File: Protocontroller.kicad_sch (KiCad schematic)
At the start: 37 parts, among them U1 AP2112K-3.3TRG1, U2 PM254-1-14-Z-8.5, U3 PM254-1-14-Z-8.5, U4 74245PW, U5 74245PW, U6 74374PW, U8 HC-JN254-2-08-W

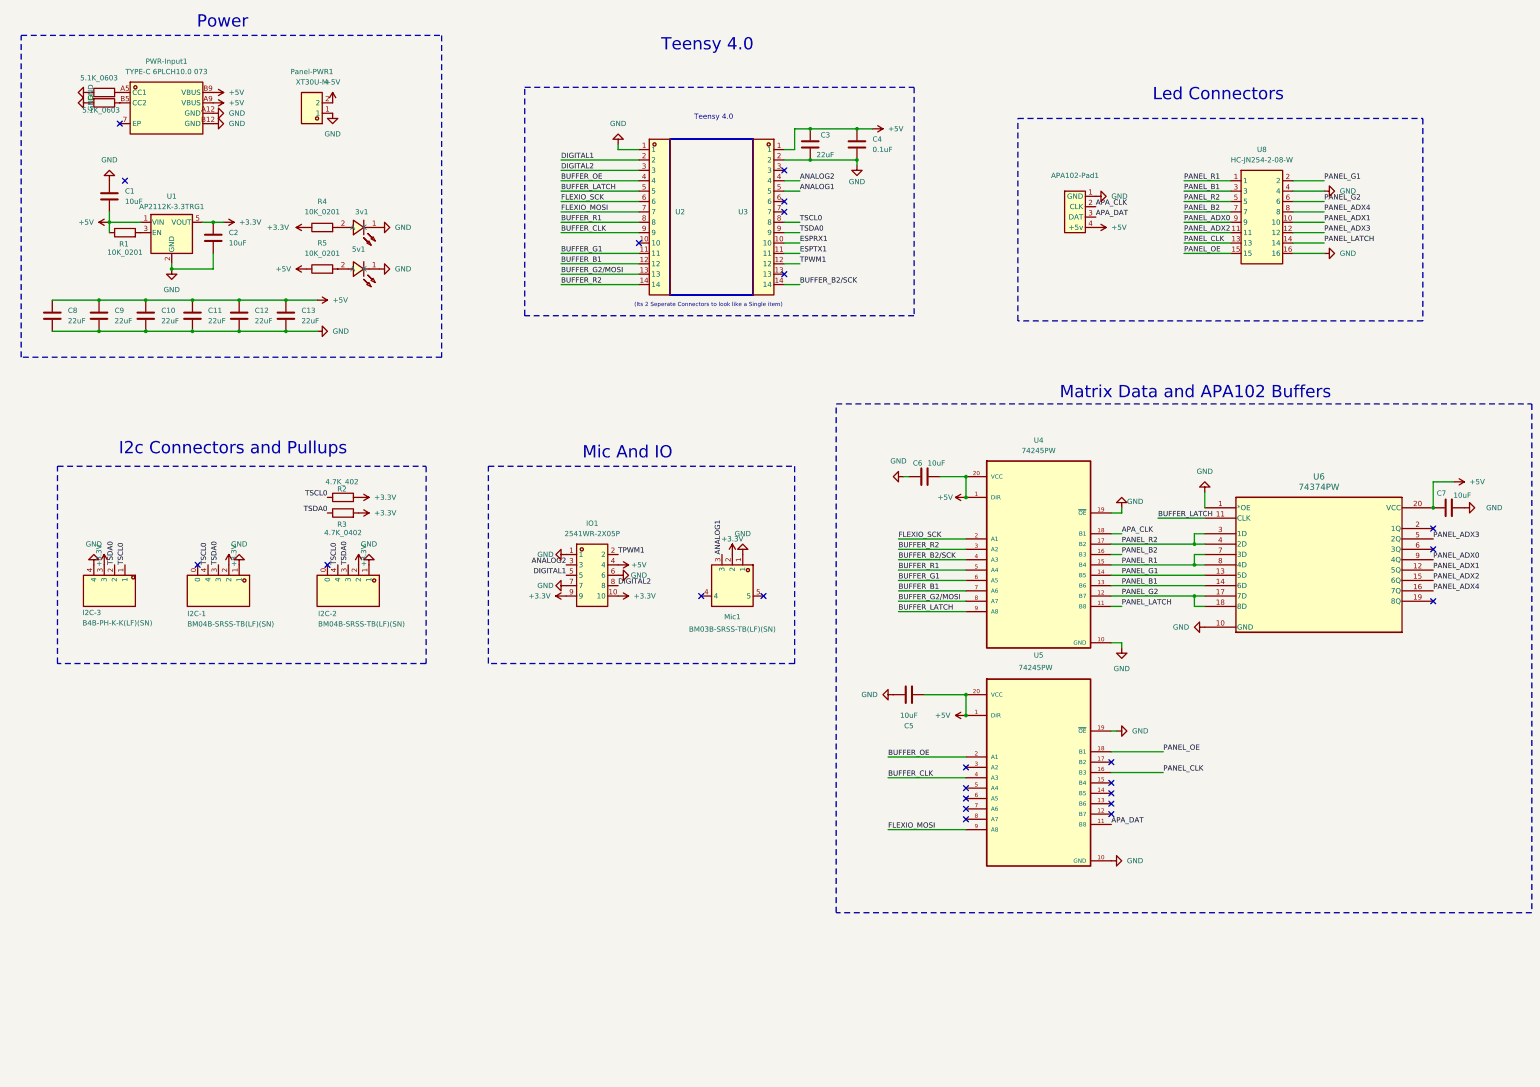
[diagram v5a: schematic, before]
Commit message: V2 of the neo released, switched stemma to stemma qt, adjusted io pinout, replaced secondary 74245 with the 7408, swapped apaclk and apadat, switched to 2 layer for cheaper costs, esp32 schematic in, in unused, dedicated fan header,
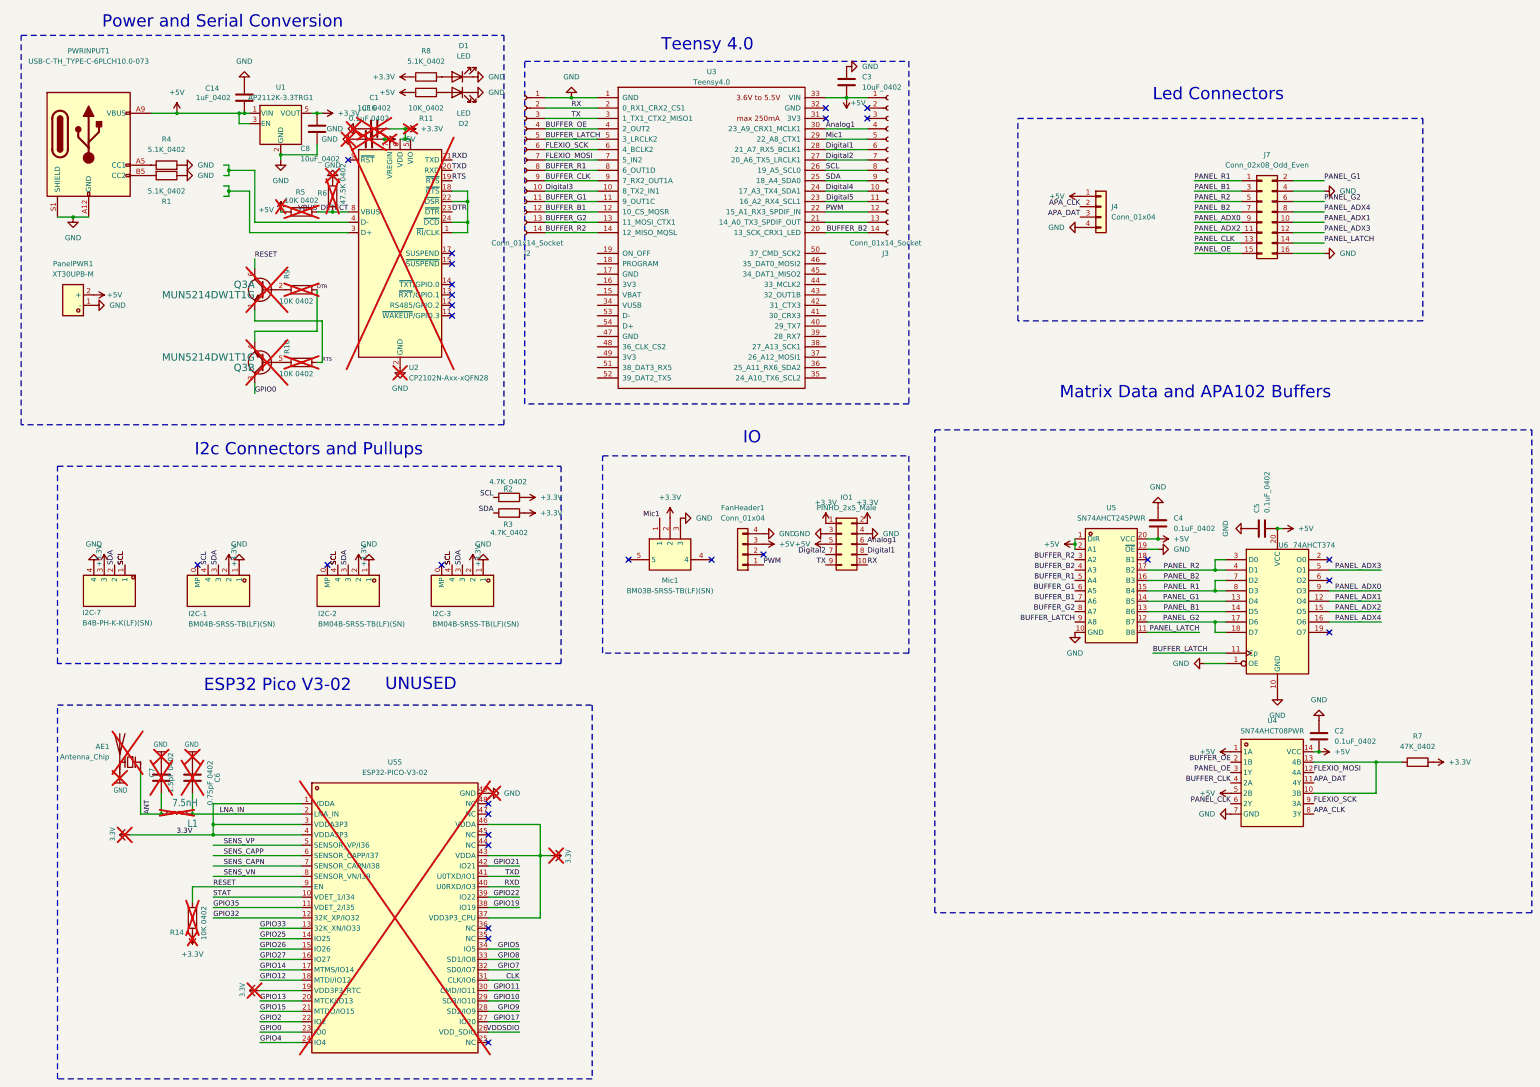
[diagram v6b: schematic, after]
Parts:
- removed 3v1, 5v1: XL-1608UVC-04, Protocontroller:LED0603-RD_PINK, symbol Protocontroller:XL-1608UVC-04
- removed APA102-Pad1: ~, Connector_Wire:JST-SM 4P PAD, symbol Protocontroller:JST-SM_4P_PAD
- removed C10, C11, C12, C13, C9: 22uF, Capacitor_SMD:C_0402_1005Metric, symbol Device:C
- removed IO1: 2541WR-2X05P, Protocontroller:HDR-TH_10P-P2.54-H-F-R2-C5-W12.7-N, symbol Protocontroller:FH-00843
- removed Mic1: BM03B-SRSS-TB(LF)(SN), Connector_JST:JST_SH_BM03B-SRSS-TB_1x03-1MP_P1.00mm_Vertical, symbol Protocontroller:SM03B-SRSS-TB(LF)(SN)(P)
- removed PWR-Input1: TYPE-C 6PLCH10.0 073, Protocontroller:USB-C-TH_TYPE-C-6PLCH10.0-073, symbol Protocontroller:TYPE-C6PLCH10.0073
- removed Panel-PWR1: XT30U-M, Connector_AMASS:AMASS_XT30U-M_1x02_P5.0mm_Vertical, symbol Protocontroller:XT30U-M
- removed U2, U3: PM254-1-14-Z-8.5, Protocontroller:HDR-TH_14P-P2.54-V-F-1, symbol Protocontroller:PM254-1-14-Z-8.5
- removed U4, U5: 74245PW, Protocontroller:SN74AHCT245PWR, symbol SN74AHCT245PWR:SN74AHCT245PWR
- removed U6: 74374PW, Protocontroller:SN74AHCT374PWR, symbol SN74HCT374DWR:SN74HCT374DWR
- removed U8: HC-JN254-2-08-W, Protocontroller:HDR-TH_16P-P2.54-H-F-R2-C8-W9.0, symbol Protocontroller:HDR-IDC-2.54-2X8P
- added AE1: Antenna_Chip, RF_Antenna:Johanson_2450AT18x100, symbol Device:Antenna_Chip
- added C14: 1uF_0402, Capacitor_SMD:C_0402_1005Metric, symbol Device:C
- added C16: 0.1uF 0402, Capacitor_SMD:C_0402_1005Metric, symbol Device:C
- added D1, D2: LED, LED_SMD:LED_0603_1608Metric, symbol Device:LED
- added FanHeader1: Conn_01x04, Connector_PinHeader_2.54mm:PinHeader_1x04_P2.54mm_Vertical, symbol Connector_Generic:Conn_01x04
- added I2C-3: BM04B-SRSS-TB(LF)(SN), Connector_JST:JST_SH_BM04B-SRSS-TB_1x04-1MP_P1.00mm_Vertical, symbol Protocontroller:BM04B-SRSS-TB(LF)(SN)
- added IO1: PINHD_2x5_Male, Connector_PinHeader_2.54mm:PinHeader_2x05_P2.54mm_Horizontal, symbol PCM_SL_Pin_Headers:PINHD_2x5_Male
- added J2, J3: Conn_01x14_Socket, Connector_PinSocket_2.54mm:PinSocket_1x14_P2.54mm_Vertical, symbol Connector:Conn_01x14_Socket
- added J4: Conn_01x04, Connector_Wire:JST_SM 1x04 Pad, symbol Connector_Generic:Conn_01x04
- added J7: Conn_02x08_Odd_Even, Connector_IDC:IDC-Header_2x08_P2.54mm_Horizontal, symbol Connector_Generic:Conn_02x08_Odd_Even
- added L1: 7.5nH, Inductor_SMD:L_0402_1005Metric, symbol Device:L
- added Mic1: BM03B-SRSS-TB(LF)(SN), Connector_JST:JST_SH_BM03B-SRSS-TB_1x03-1MP_P1.00mm_Vertical, symbol Protocontroller:BM03B-SRSS-TB(LF)(SN)
- added PWRINPUT1: USB-C-TH_TYPE-C-6PLCH10.0-073, Protocontroller:USB-C-TH_TYPE-C-6PLCH10.0-073, symbol Connector:USB_C_Receptacle_PowerOnly_6P
- added PanelPWR1: XT30UPB-M, Connector_AMASS:AMASS_XT30UPB-M_1x02_P5.0mm_Vertical, symbol Protocontroller:XT30UPB-M
- added Q3: MUN5214DW1T1G, Package_TO_SOT_SMD:SOT-363_SC-70-6, symbol Transistor_BJT:MBT3904DW1
- added R10, R14, R9: 10K 0402, Resistor_SMD:R_0402_1005Metric, symbol Device:R
- added R11: 10K_0402, Resistor_SMD:R_0402_1005Metric, symbol Device:R
- added R8: 5.1K_0402, Resistor_SMD:R_0402_1005Metric, symbol Device:R
- added U2: CP2102N-Axx-xQFN28, Package_DFN_QFN:QFN-24-1EP_4x4mm_P0.5mm_EP2.6x2.6mm, symbol Interface_USB:CP2102N-Axx-xQFN24
- added U3: Teensy4.0, Teensy:Teensy40_SMT, symbol Teensy:Teensy4.0
- added U4: SN74AHCT08PWR, Protocontroller:TSSOP-14_L5.0-W4.4-P0.65-LS6.4-BL, symbol Protocontroller:SN74AHCT08PWR
- added U5: SN74AHCT245PWR, Protocontroller:TSSOP-20_L6.5-W4.4-P0.65-LS6.4-BL, symbol Protocontroller:SN74AHCT245PWR
- added U55: ESP32-PICO-V3-02, Protocontroller:QFN-48_L7.0-W7.0-P0.50-BL-EP5.1, symbol ESP32-BT:ESP32-PICO-V3-02
- added U6: 74AHCT374, Protocontroller:SN74AHCT374PWR, symbol 74xx:74AHCT374
- C1: value 10uF -> 1uF 0402; footprint Capacitor_SMD:C_0603_1608Metric -> Capacitor_SMD:C_0402_1005Metric; LCSC Part C19702 -> (none); now not fitted; now left out of the parts list
- C2, C5: value 10uF -> 0.1uF_0402; footprint Capacitor_SMD:C_0603_1608Metric -> Capacitor_SMD:C_0402_1005Metric; JLC (none) -> C1525; LCSC Part C19702 -> (none)
- C3: value 22uF -> 10uF_0402; footprint Capacitor_SMD:C_0603_1608Metric -> Capacitor_SMD:C_0402_1005Metric; JLC (none) -> C15525; LCSC Part C59461 -> (none)
- C4: value 0.1uF -> 0.1uF_0402; footprint Capacitor_SMD:C_0603_1608Metric -> Capacitor_SMD:C_0402_1005Metric; JLC (none) -> C1525; LCSC Part C14663 -> (none)
- C6: value 10uF -> 0.75pF 0402; footprint Capacitor_SMD:C_0603_1608Metric -> Capacitor_SMD:C_0402_1005Metric; LCSC Part C19702 -> (none); now not fitted; now left out of the parts list
- C7: value 10uF -> 1.5pF 0402; footprint Capacitor_SMD:C_0603_1608Metric -> Capacitor_SMD:C_0402_1005Metric; LCSC Part C19702 -> (none); now not fitted; now left out of the parts list
- C8: value 22uF -> 10uF_0402; JLC (none) -> C15525; LCSC Part C415703 -> (none)
- I2C-1, I2C-2: footprint Protocontroller:CONN-SMD_BM04B-SRSS-TB -> Connector_JST:JST_SH_BM04B-SRSS-TB_1x04-1MP_P1.00mm_Vertical
- R1, R4: value 10K_0201 -> 5.1K_0402; footprint Resistor_SMD:R_0201_0603Metric -> Resistor_SMD:R_0402_1005Metric; JLC (none) -> C25905; LCSC Part C106225 -> (none)
- R2: value 4.7K_402 -> 4.7K_0402
- R5: value 10K_0201 -> 10K 0402; footprint Resistor_SMD:R_0201_0603Metric -> Resistor_SMD:R_0402_1005Metric; LCSC Part C106225 -> (none); now not fitted; now left out of the parts list
- R6: value 5.1K_0603 -> 47.5K 0402; footprint Resistor_SMD:R_0603_1608Metric -> Resistor_SMD:R_0402_1005Metric; LCSC Part C23186 -> (none); now not fitted; now left out of the parts list
- R7: value 5.1K_0603 -> 47K_0402; footprint Resistor_SMD:R_0603_1608Metric -> Resistor_SMD:R_0402_1005Metric; JLC (none) -> C25792; LCSC Part C23186 -> (none)
- U1: LCSC Part C51118 -> (none)
- renumbered I2C-3 to I2C-7
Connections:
- net +3.3V: now also C1.2, C8.1, R7.2, I2C-3.2, IO1.1, IO1.2, Mic1.2, R14.1, R8.1, U2.5 (VIO), U2.6 (VDD); no longer C2.1, R4.1
- net +5V: now also C2.2, C3.2, C4.2, U1.3 (EN), C14.1, C16.2, FanHeader1.3 (Pin_3), IO1.5, J3.1 (Pin_1), J4.1 (Pin_1), PWRINPUT1.A9 (VBUS), PWRINPUT1.B9 (VBUS), PanelPWR1.2 (+), R11.1, U2.7 (VREGIN), U3.33 (VIN), U4.1 (1A), U4.14 (VCC), U4.5 (2B), U5.1 (DIR), U5.2 (A1), U5.20 (VCC), U6.20 (VCC); no longer C1.2, C3.1, C4.1, C6.2, C7.2, C8.1, R1.1
- net APA_CLK: now also J4.2 (Pin_2), U4.8 (3Y)
- net APA_DAT: now also J4.3 (Pin_3), U4.11 (4Y)
- net BUFFER_B1: now also J2.12 (Pin_12), U3.12 (10_CS_MQSR), U5.7 (A6)
- net BUFFER_CLK: now also J2.9 (Pin_9), U3.9 (7_RX2_OUT1A), U4.4 (2A)
- net BUFFER_G1: now also J2.11 (Pin_11), U3.11 (9_OUT1C), U5.6 (A5)
- net BUFFER_LATCH: now also J2.5 (Pin_5), U3.5 (3_LRCLK2), U5.9 (A8), U6.11 (Cp)
- net BUFFER_OE: now also J2.4 (Pin_4), U3.4 (2_OUT2), U4.2 (1B)
- net BUFFER_R1: now also J2.8 (Pin_8), U3.8 (6_OUT1D), U5.5 (A4)
- net BUFFER_R2: now also J2.14 (Pin_14), U3.14 (12_MISO_MQSL), U5.3 (A2)
- net FLEXIO_MOSI: now also J2.7 (Pin_7), U3.7 (5_IN2), U4.12 (4A)
- net FLEXIO_SCK: now also J2.6 (Pin_6), U3.6 (4_BCLK2), U4.9 (3A)
- net GND: now also C2.1, C3.1, C4.1, C6.2, R1.1, R4.2, R6.1, AE1.2 (PCB_Trace), C14.2, C16.1, D1.1 (K), D2.1 (K), FanHeader1.4 (Pin_4), I2C-3.1, IO1.3, IO1.4, J2.1 (Pin_1), J4.4 (Pin_4), J7.16 (Pin_16), J7.4 (Pin_4), Mic1.3, PWRINPUT1.A12 (GND), PWRINPUT1.B12 (GND), PWRINPUT1.S1 (SHIELD), PanelPWR1.1 (-), U2.2 (GND), U2.25 (GND), U3.1 (GND), U4.7 (GND), U5.10 (GND), U5.19 (~{OE}), U55.49 (GND), U6.1 (OE), U6.10 (GND); no longer C2.2, C3.2, C4.2, C6.1, R6.2, R7.1
- net PANEL_ADX0: now also J7.9 (Pin_9), U6.9 (O3)
- net PANEL_ADX1: now also J7.10 (Pin_10), U6.12 (O4)
- net PANEL_ADX2: now also J7.11 (Pin_11), U6.15 (O5)
- net PANEL_ADX3: now also J7.12 (Pin_12), U6.5 (O1)
- net PANEL_ADX4: now also J7.8 (Pin_8), U6.16 (O6)
- net PANEL_B1: now also J7.3 (Pin_3), U5.13 (B6), U6.14 (D5)
- net PANEL_B2: now also J7.7 (Pin_7), U5.16 (B3)
- net PANEL_CLK: now also J7.13 (Pin_13), U4.6 (2Y)
- net PANEL_G1: now also J7.2 (Pin_2), U5.14 (B5), U6.13 (D4)
- net PANEL_G2: now also J7.6 (Pin_6), U5.12 (B7), U6.17 (D6), U6.18 (D7)
- net PANEL_LATCH: now also J7.14 (Pin_14), U5.11 (B8)
- net PANEL_OE: now also J7.15 (Pin_15), U4.3 (1Y)
- net PANEL_R1: now also J7.1 (Pin_1), U5.15 (B4), U6.7 (D2), U6.8 (D3)
- net PANEL_R2: now also J7.5 (Pin_5), U5.17 (B2), U6.3 (D0), U6.4 (D1)
- net at R1.2: now also PWRINPUT1.B5 (CC2); no longer U1.3 (EN)
- net VBUS_DETECT: now reaches R5.2
- net VBUS_DETECT: now also R6.2, U2.8 (VBUS)
- net TSCL0 renamed SCL
- net SCL: now also I2C-3.4, J3.8 (Pin_8), U3.26 (19_A5_SCL0)
- net TSDA0 renamed SDA
- net SDA: now also I2C-3.3, J3.9 (Pin_9), U3.25 (18_A4_SDA0)
- new net: U2.1 (~{RI}/CLK), U2.18 (~{CTS}), U2.22 (~{DSR}), U2.24 (~{DCD})
- new net: PWRINPUT1.A5 (CC1), R4.1
- new net: Q3.5 (B2), R10.1
- new net: J3.13 (Pin_13), U3.21 (14_A0_TX3_SPDIF_OUT)
- new net: R7.1, U4.10 (3B), U4.13 (4B)
- new net: Q3.2 (B1), R9.1
- new net: D2.2 (A), R11.2
- new net: D1.2 (A), R8.2
- new net 3.3V: U55.1 (VDDA), U55.19 (VDD3P3_RTC), U55.3 (VDDA3P3), U55.37 (VDD3P3_CPU), U55.4 (VDDA3P3), U55.43 (VDDA), U55.46 (VDDA)
- new net ANT: AE1.1 (FEED), C7.2, L1.1
- new net Analog1: IO1.6, J3.4 (Pin_4), U3.30 (23_A9_CRX1_MCLK1)
- new net BUFFER_B2: J3.14 (Pin_14), U3.20 (13_SCK_CRX1_LED), U5.4 (A3)
- new net BUFFER_G2: J2.13 (Pin_13), U3.13 (11_MOSI_CTX1), U5.8 (A7)
- new net CLK: U55.31 (CLK/IO6)
- new net DTR: Q3.4 (E2), R9.2, U2.23 (~{DTR})
- new net Digital1: IO1.8, J3.6 (Pin_6), U3.28 (21_A7_RX5_BCLK1)
- new net Digital2: IO1.7, J3.7 (Pin_7), U3.27 (20_A6_TX5_LRCLK1)
- new net Digital3: J2.10 (Pin_10), U3.10 (8_TX2_IN1)
- new net Digital4: J3.10 (Pin_10), U3.24 (17_A3_TX4_SDA1)
- new net Digital5: J3.11 (Pin_11), U3.23 (16_A2_RX4_SCL1)
- new net GPIO0: Q3.3 (C2), U55.23 (IO0)
- new net GPIO10: U55.29 (SD3/IO10)
- new net GPIO11: U55.30 (CMD/IO11)
- new net GPIO12: U55.18 (MTDI/IO12)
- new net GPIO13: U55.20 (MTCK/IO13)
- new net GPIO14: U55.17 (MTMS/IO14)
- new net GPIO15: U55.21 (MTDO/IO15)
- new net GPIO17: U55.27 (IO20)
- new net GPIO19: U55.38 (IO19)
- new net GPIO2: U55.22 (IO2)
- new net GPIO21: U55.42 (IO21)
- new net GPIO22: U55.39 (IO22)
- new net GPIO25: U55.14 (IO25)
- new net GPIO26: U55.15 (IO26)
- new net GPIO27: U55.16 (IO27)
- new net GPIO32: U55.12 (32K_XP/IO32)
- new net GPIO33: U55.13 (32K_XN/IO33)
- new net GPIO35: U55.11 (VDET_2/I35)
- new net GPIO4: U55.24 (IO4)
- new net GPIO5: U55.34 (IO5)
- new net GPIO7: U55.32 (SD0/IO7)
- new net GPIO8: U55.33 (SD1/IO8)
- new net GPIO9: U55.28 (SD2/IO9)
- new net LNA_IN: C6.1, L1.2, U55.2 (LNA_IN)
- new net Mic1: J3.5 (Pin_5), Mic1.1, U3.29 (22_A8_CTX1)
- new net PWM: FanHeader1.1 (Pin_1), J3.12 (Pin_12), U3.22 (15_A1_RX3_SPDIF_IN)
- new net RESET: Q3.6 (C1), R14.2, U55.9 (EN)
- new net RTS: Q3.1 (E1), R10.2, U2.19 (~{RTS})
- new net RX: IO1.10, J2.2 (Pin_2), U3.2 (0_RX1_CRX2_CS1)
- new net RXD: U2.21 (TXD), U55.40 (U0RXD/IO3)
- new net SENS_CAPN: U55.7 (SENSOR_CAPN/I38)
- new net SENS_CAPP: U55.6 (SENSOR_CAPP/I37)
- new net SENS_VN: U55.8 (SENSOR_VN/I39)
- new net SENS_VP: U55.5 (SENSOR_VP/I36)
- new net STAT: U55.10 (VDET_1/I34)
- new net TX: IO1.9, J2.3 (Pin_3), U3.3 (1_TX1_CTX2_MISO1)
- new net TXD: U2.20 (RXD), U55.41 (U0TXD/IO1)
- new net VDDSDIO: U55.26 (VDD_SDIO)
- no-connect marks 24 -> 28
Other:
- note added: "ESP32 Pico V3-02"
- note added: "IO"
- note added: "Power and Serial Conversion"
- note added: "UNUSED"
- note removed: "(Its 2 Seperate Connectors to look like a Single item)"
- note removed: "Mic And IO"
- note removed: "Power"
- moved on the sheet: R2, R3

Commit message: new layout, bunch of empty space
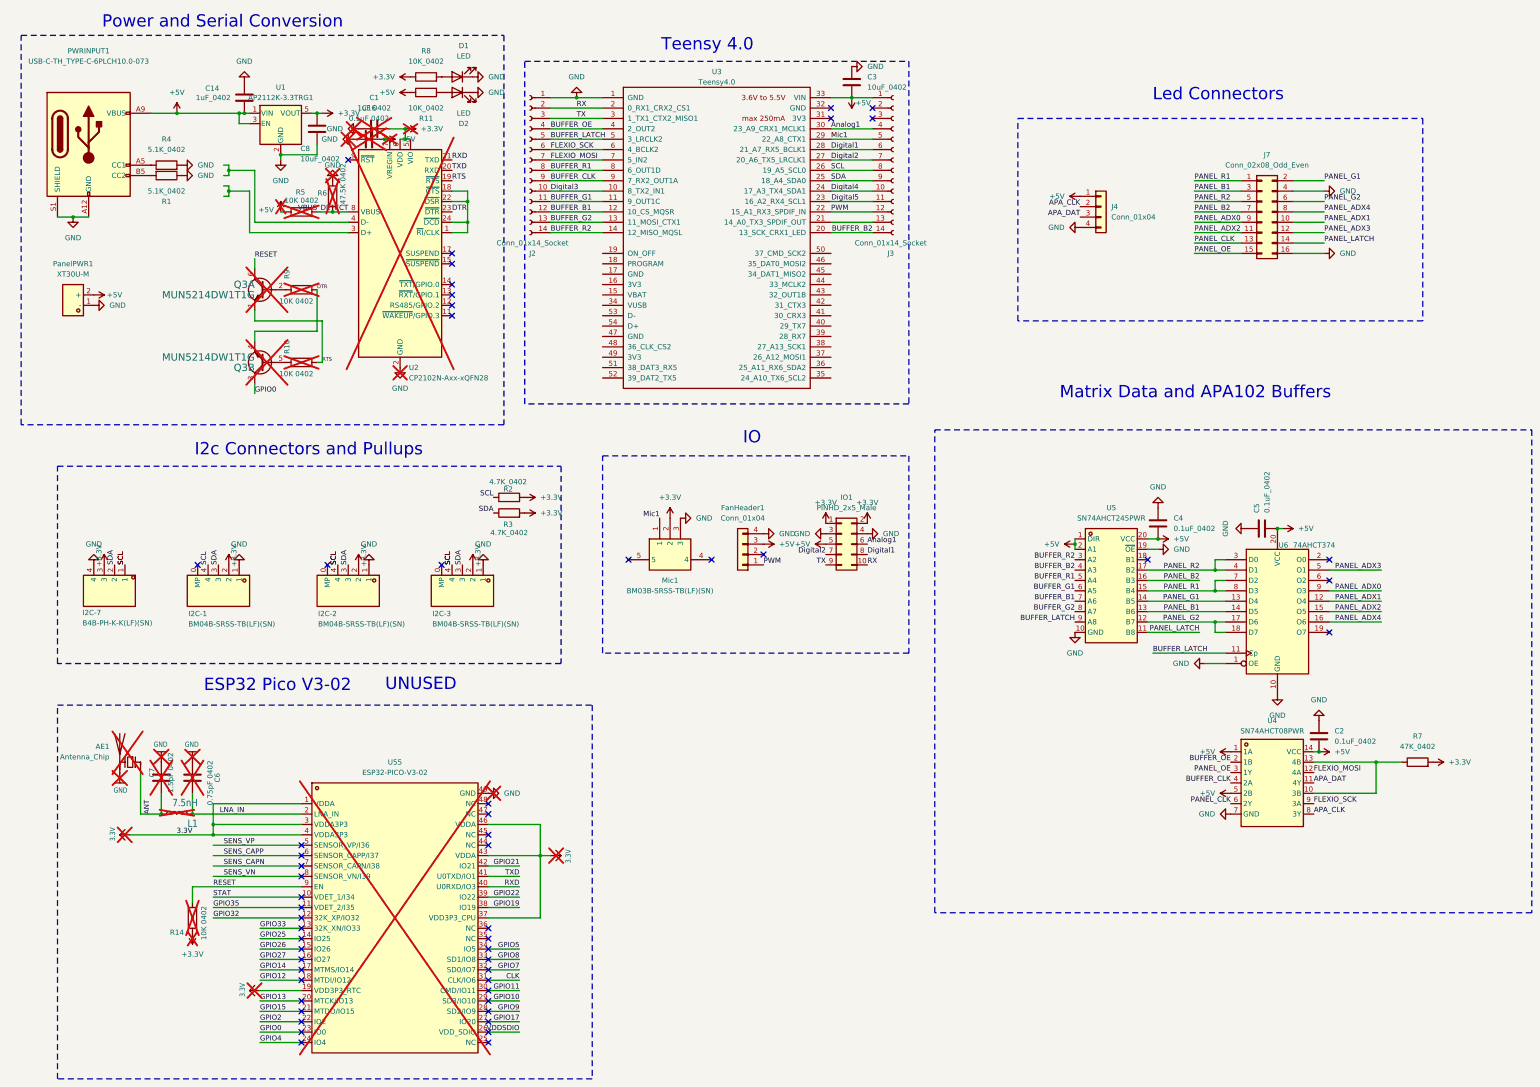
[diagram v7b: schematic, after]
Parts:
- AE1: footprint RF_Antenna:Johanson_2450AT18x100 -> Resistor_SMD:R_0805_2012Metric; LCSC Part (none) -> C2925419
- PWRINPUT1: footprint Protocontroller:USB-C-TH_TYPE-C-6PLCH10.0-073 -> Protocontroller:USB-C-TH_TYPE-C-6P-LC6.8-073; JLC C5156601 -> C2858272
- PanelPWR1: value XT30UPB-M -> XT30U-M; footprint Connector_AMASS:AMASS_XT30UPB-M_1x02_P5.0mm_Vertical -> Connector_AMASS:AMASS_XT30U-M_1x02_P5.0mm_Vertical
- R8: value 5.1K_0402 -> 10K_0402; JLC C25905 -> C25744
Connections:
- no-connect marks 28 -> 55
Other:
- moved on the sheet: C3, J2, J3, U3

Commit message: fix files
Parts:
- removed AE1: Antenna_Chip, Resistor_SMD:R_0805_2012Metric, symbol Device:Antenna_Chip
- removed C1: 1uF 0402, Capacitor_SMD:C_0402_1005Metric, symbol Device:C
- removed C16: 0.1uF 0402, Capacitor_SMD:C_0402_1005Metric, symbol Device:C
- removed C6: 0.75pF 0402, Capacitor_SMD:C_0402_1005Metric, symbol Device:C
- removed C7: 1.5pF 0402, Capacitor_SMD:C_0402_1005Metric, symbol Device:C
- removed I2C-7: B4B-PH-K-K(LF)(SN), Protocontroller:CONN-TH_B4B-PH-K-S-LF-SN, symbol Protocontroller:B4B-PH-K-K(LF)(SN)
- removed L1: 7.5nH, Inductor_SMD:L_0402_1005Metric, symbol Device:L
- removed PWRINPUT1: USB-C-TH_TYPE-C-6PLCH10.0-073, Protocontroller:USB-C-TH_TYPE-C-6P-LC6.8-073, symbol Connector:USB_C_Receptacle_PowerOnly_6P
- removed Q3: MUN5214DW1T1G, Package_TO_SOT_SMD:SOT-363_SC-70-6, symbol Transistor_BJT:MBT3904DW1
- removed R10, R14, R5, R9: 10K 0402, Resistor_SMD:R_0402_1005Metric, symbol Device:R
- removed R6: 47.5K 0402, Resistor_SMD:R_0402_1005Metric, symbol Device:R
- removed U2: CP2102N-Axx-xQFN28, Package_DFN_QFN:QFN-24-1EP_4x4mm_P0.5mm_EP2.6x2.6mm, symbol Interface_USB:CP2102N-Axx-xQFN24
- removed U55: ESP32-PICO-V3-02, Protocontroller:QFN-48_L7.0-W7.0-P0.50-BL-EP5.1, symbol ESP32-BT:ESP32-PICO-V3-02
- added J1: USB_C_Receptacle_USB2.0_16P, Protocontroller:USB-TH_TYPE-C-16PFS-LCH7.45-IPX8, symbol Connector:USB_C_Receptacle_USB2.0_16P
- C14: JLC C52923 -> (none); LCSC Part (none) -> C52923
- C2, C4, C5: value 0.1uF_0402 -> 100nF_0402
- C3: JLC C15525 -> (none); LCSC Part (none) -> C15525
- FanHeader1: now left out of the parts list
- I2C-1, I2C-2, I2C-3: footprint Connector_JST:JST_SH_BM04B-SRSS-TB_1x04-1MP_P1.00mm_Vertical -> Protocontroller:CONN-SMD_BM04B-SRSS-TB
- PanelPWR1: value XT30U-M -> XT30U-M.G.B; LCSC Part C428721 -> C19268020
- R1, R4: JLC C25905 -> (none); LCSC Part (none) -> C25905
- R11, R8: JLC C25744 -> (none); LCSC Part (none) -> C25744
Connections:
- net +3.3V: now also R7.1; no longer R7.2
- net +5V: now also J1.A4 (VBUS), J1.A9 (VBUS), J1.B4 (VBUS), J1.B9 (VBUS)
- net GND: now also I2C-2.MP, J1.A1 (GND), J1.A12 (GND), J1.B1 (GND), J1.B12 (GND), J1.S1 (SHIELD)
- net at R1.2: now also J1.B5 (CC2)
- net at R4.1: now also J1.A5 (CC1)
- net at U4.10 (3B), U4.13 (4B): now also R7.2; no longer R7.1
- no-connect marks 55 -> 20
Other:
- note removed: "ESP32 Pico V3-02"
- note removed: "UNUSED"
- moved on the sheet: C3, I2C-1, I2C-2, I2C-3, J2, J3, PanelPWR1, R1, R4, R7, U3
